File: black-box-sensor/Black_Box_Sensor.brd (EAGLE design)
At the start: 100 x 80 mm, 4 parts, among them U1 ADXL375, U2 ADXL375, U3 ATMEGA32U4-AU, U4 FXAS21002CQR1

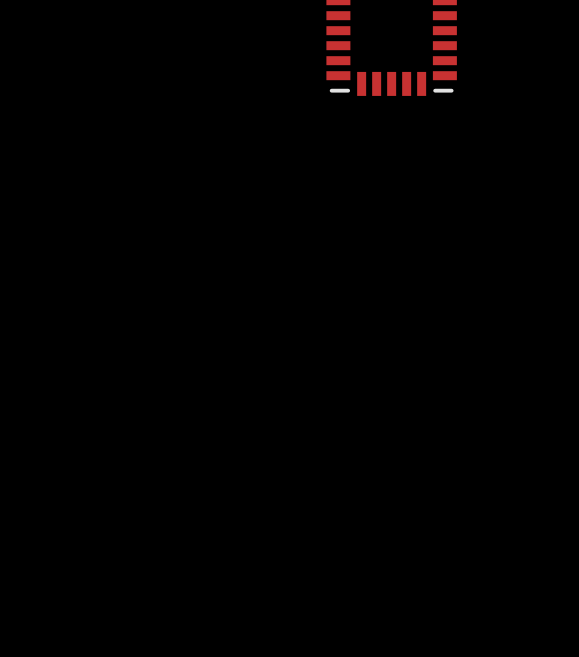
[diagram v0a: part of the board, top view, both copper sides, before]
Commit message: voltage regulator addition
added voltage reg to the library, and added appropriate parts to the schematic for the voltage regulator to work
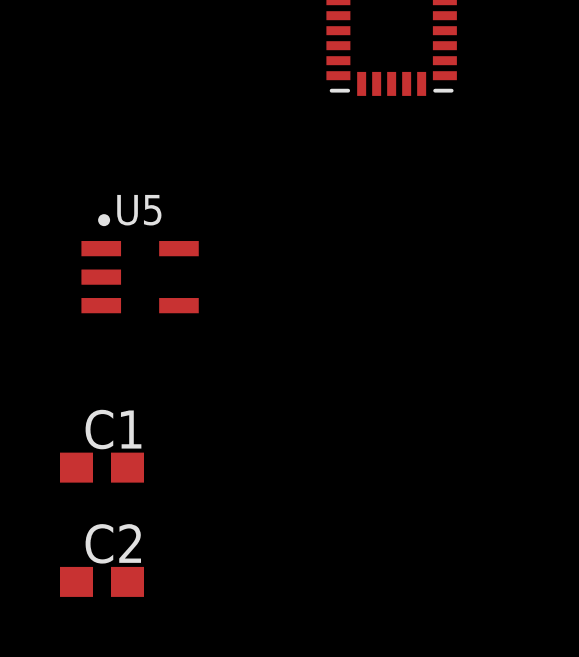
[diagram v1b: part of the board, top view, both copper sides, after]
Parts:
- added C1, C2: 1µF, rcl:C0603
- added U5: MIC5504-3.3YM5-TR, BBS_Library:SOT-23-5_MC_MCH
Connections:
- new net +3.3V: C2.1, U5.5
- new net GND: C1.2, C2.2, U5.2
- new net VBATT: C1.1, U5.1, U5.3
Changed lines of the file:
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@@
 <?xml version="1.0" encoding="utf-8"?>
 <!DOCTYPE eagle SYSTEM "eagle.dtd">
-<eagle version="9.6.2">
+<eagle version="9.5.1">
 <drawing>
 <settings>
@@
 <layers>
 <layer number="1" name="Top" color="4" fill="1" visible="yes" active="yes"/>
+<layer number="2" name="Route2" color="16" fill="1" visible="no" active="no"/>
+<layer number="3" name="Route3" color="17" fill="1" visible="no" active="no"/>
+<layer number="4" name="Route4" color="18" fill="1" visible="no" active="no"/>
+<layer number="5" name="Route5" color="19" fill="1" visible="no" active="no"/>
+<layer number="6" name="Route6" color="25" fill="1" visible="no" active="no"/>
+<layer number="7" name="Route7" color="26" fill="1" visible="no" active="no"/>
+<layer number="8" name="Route8" color="27" fill="1" visible="no" active="no"/>
+<layer number="9" name="Route9" color="28" fill="1" visible="no" active="no"/>
+<layer number="10" name="Route10" color="29" fill="1" visible="no" active="no"/>
+<layer number="11" name="Route11" color="30" fill="1" visible="no" active="no"/>
+<layer number="12" name="Route12" color="20" fill="1" visible="no" active="no"/>
+<layer number="13" name="Route13" color="21" fill="1" visible="no" active="no"/>
+<layer number="14" name="Route14" color="22" fill="1" visible="no" active="no"/>
+<layer number="15" name="Route15" color="23" fill="1" visible="no" active="no"/>
 <layer number="16" name="Bottom" color="1" fill="1" visible="yes" active="yes"/>
 <layer number="17" name="Pads" color="2" fill="1" visible="yes" active="yes"/>
@@
 <attribute name="VALUE" x="-4.275" y="-41.775" size="1" layer="27" font="vector" ratio="10" align="top-left"/>
 </element>
+<element name="U5" library="BBS_Library" package="SOT-23-5_MC_MCH" value="MIC5504-3.3YM5-TR" x="-10.16" y="-46.99" smashed="yes">
+<attribute name="DKPN" value="576-4764-1-ND" x="-10.16" y="-46.99" size="1.778" layer="27" display="off"/>
+<attribute name="NAME" x="-11.03" y="-45.25" size="1" layer="25" font="vector" ratio="10"/>
+<attribute name="VALUE" x="-11.13" y="-48.8" size="1" layer="27" font="vector" ratio="10" align="top-left"/>
+</element>
+<element name="C1" library="rcl" library_urn="urn:adsk.eagle:library:334" package="C0603" package3d_urn="urn:adsk.eagle:package:23616/2" value="1µF" x="-11.43" y="-53.34" smashed="yes">
+<attribute name="DKPN" value="CC0603KRX7R6BB105" x="-11.43" y="-53.34" size="1.778" layer="27" display="off"/>
+<attribute name="NAME" x="-12.065" y="-52.705" size="1.27" layer="25"/>
+<attribute name="POPULARITY" value="37" x="-11.43" y="-53.34" size="1.778" layer="27" display="off"/>
+<attribute name="SPICEPREFIX" value="C" x="-11.43" y="-53.34" size="1.778" layer="27" display="off"/>
+<attribute name="VALUE" x="-12.065" y="-55.245" size="1.27" layer="27"/>
+<attribute name="VOLTAGE" value="10V" x="-11.43" y="-53.34" size="1.778" layer="27" display="off"/>
+</element>
+<element name="C2" library="rcl" library_urn="urn:adsk.eagle:library:334" package="C0603" package3d_urn="urn:adsk.eagle:package:23616/2" value="1µF" x="-11.43" y="-57.15" smashed="yes">
+<attribute name="DKPN" value="CC0603KRX7R6BB105" x="-11.43" y="-57.15" size="1.778" layer="27" display="off"/>
+<attribute name="NAME" x="-12.065" y="-56.515" size="1.27" layer="25"/>
+<attribute name="POPULARITY" value="37" x="-11.43" y="-57.15" size="1.778" layer="27" display="off"/>
+<attribute name="SPICEPREFIX" value="C" x="-11.43" y="-57.15" size="1.778" layer="27" display="off"/>
+<attribute name="VALUE" x="-12.065" y="-59.055" size="1.27" layer="27"/>
+<attribute name="VOLTAGE" value="10V" x="-11.43" y="-57.15" size="1.778" layer="27" display="off"/>
+</element>
 </elements>
 <signals>
+<signal name="GND">
+<contactref element="U5" pad="2"/>
+<contactref element="C1" pad="2"/>
+<contactref element="C2" pad="2"/>
+<wire x1="-10.58" y1="-53.34" x2="-10.58" y2="-57.15" width="0" layer="19" extent="1-1"/>
+<wire x1="-11.4554" y1="-46.99" x2="-10.58" y2="-53.34" width="0" layer="19" extent="1-1"/>
+</signal>
+<signal name="VBATT">
+<contactref element="U5" pad="1"/>
+<contactref element="C1" pad="1"/>
+<contactref element="U5" pad="3"/>
+<wire x1="-11.4554" y1="-47.94" x2="-12.28" y2="-53.34" width="0" layer="19" extent="1-1"/>
+<wire x1="-11.4554" y1="-46.04" x2="-11.4554" y2="-47.94" width="0" layer="19" extent="1-1"/>
+</signal>
+<signal name="+3.3V">
+<contactref element="U5" pad="5"/>
+<contactref element="C2" pad="1"/>
+<wire x1="-8.8646" y1="-46.04" x2="-12.28" y2="-57.15" width="0" layer="19" extent="1-1"/>
+</signal>
 </signals>
 <mfgpreviewcolors>
@@
 </board>
 </drawing>
+<compatibility>
+<note version="8.2" severity="warning">
+Since Version 8.2, EAGLE supports online libraries. The ids
+of those online libraries will not be understood (or retained)
+with this version.
+</note>
+<note version="8.3" severity="warning">
+Since Version 8.3, EAGLE supports URNs for individual library
+assets (packages, symbols, and devices). The URNs of those assets
+will not be understood (or retained) with this version.
+</note>
+<note version="8.3" severity="warning">
+Since Version 8.3, EAGLE supports the association of 3D packages
+with devices in libraries, schematics, and board files. Those 3D
+packages will not be understood (or retained) with this version.
+</note>
+</compatibility>
 </eagle>

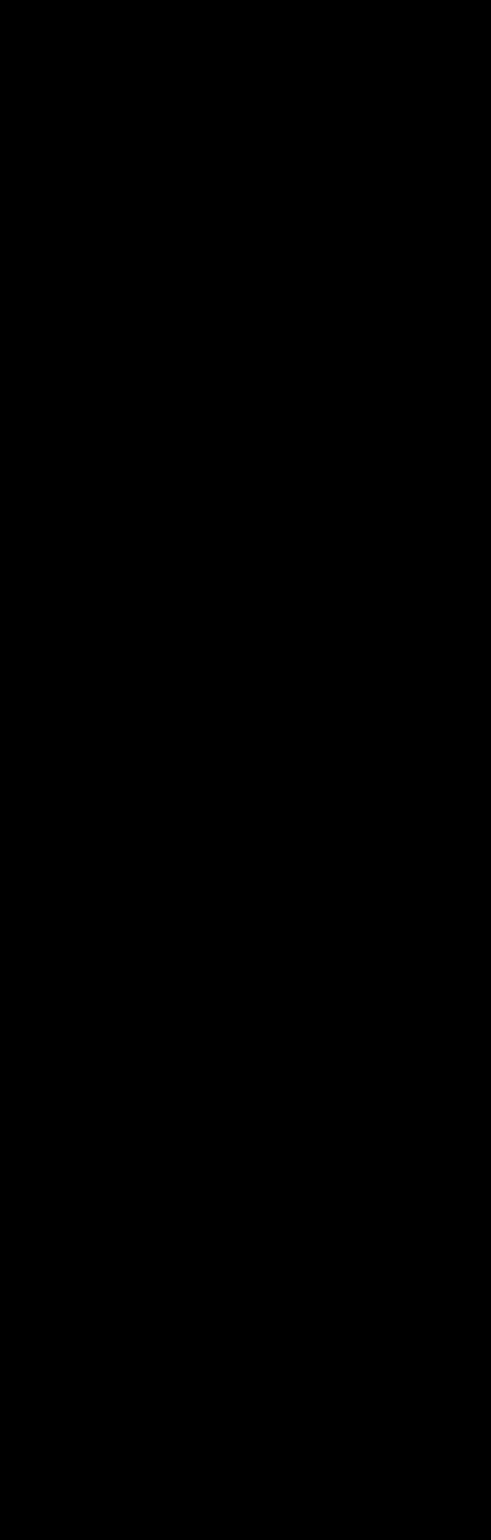
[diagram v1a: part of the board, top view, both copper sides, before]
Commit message: start schematic for accelerometer and gyro
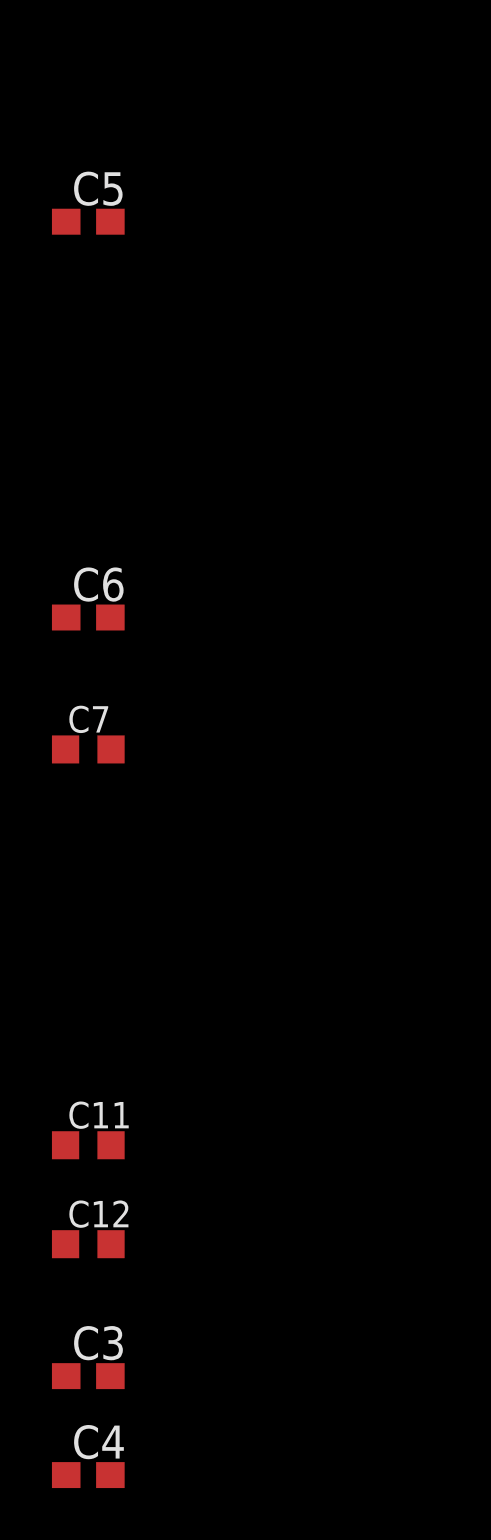
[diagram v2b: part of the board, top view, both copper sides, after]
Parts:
- added C11, C12: 0.1uF, rcl:C0603K
- added C3, C4: 0.1uF, rcl:C0603
- added C5: 10uF, rcl:C0603
- added C6: 100nF, rcl:C0603
- added C7: 1uF, rcl:C0603K
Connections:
- new net 3.3V: C11.1, C4.1, C7.1, U1.1, U4.15
- new net N$1: C6.1, U4.16
- new net N$2: C3.1, C5.1
- new net N$3: C12.1, U4.18, U4.8
- net GND: now also C11.2, C12.2, C3.2, C4.2, C5.2, C6.2, C7.2, U1.2, U1.4, U1.5, U1.6, U4.1, U4.10, U4.14, U4.19, U4.20, U4.21, U4.22, U4.23, U4.24, U4.5, U4.6, U4.7, U4.9
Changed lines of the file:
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@@
 <?xml version="1.0" encoding="utf-8"?>
 <!DOCTYPE eagle SYSTEM "eagle.dtd">
-<eagle version="9.5.1">
+<eagle version="9.6.2">
 <drawing>
 <settings>
@@
 <attribute name="VOLTAGE" value="10V" x="-11.43" y="-57.15" size="1.778" layer="27" display="off"/>
 </element>
+<element name="C5" library="rcl" library_urn="urn:adsk.eagle:library:334" package="C0603" package3d_urn="urn:adsk.eagle:package:23616/2" value="10uF" x="-11.43" y="-71.12" smashed="yes">
+<attribute name="NAME" x="-12.065" y="-70.485" size="1.27" layer="25"/>
+<attribute name="POPULARITY" value="37" x="-11.43" y="-71.12" size="1.778" layer="27" display="off"/>
+<attribute name="SPICEPREFIX" value="C" x="-11.43" y="-71.12" size="1.778" layer="27" display="off"/>
+<attribute name="VALUE" x="-12.065" y="-73.025" size="1.27" layer="27"/>
+</element>
+<element name="C6" library="rcl" library_urn="urn:adsk.eagle:library:334" package="C0603" package3d_urn="urn:adsk.eagle:package:23616/2" value="100nF" x="-11.43" y="-86.36" smashed="yes">
+<attribute name="NAME" x="-12.065" y="-85.725" size="1.27" layer="25"/>
+<attribute name="POPULARITY" value="37" x="-11.43" y="-86.36" size="1.778" layer="27" display="off"/>
+<attribute name="SPICEPREFIX" value="C" x="-11.43" y="-86.36" size="1.778" layer="27" display="off"/>
+<attribute name="VALUE" x="-12.065" y="-88.265" size="1.27" layer="27"/>
+</element>
+<element name="C7" library="rcl" library_urn="urn:adsk.eagle:library:334" package="C0603K" package3d_urn="urn:adsk.eagle:package:23680/2" value="1uF" x="-11.43" y="-91.44" smashed="yes">
+<attribute name="NAME" x="-12.23" y="-90.79" size="1.016" layer="25"/>
+<attribute name="POPULARITY" value="5" x="-11.43" y="-91.44" size="1.778" layer="27" display="off"/>
+<attribute name="SPICEPREFIX" value="C" x="-11.43" y="-91.44" size="1.778" layer="27" display="off"/>
+<attribute name="VALUE" x="-12.23" y="-93.09" size="1.016" layer="27"/>
+</element>
+<element name="C11" library="rcl" library_urn="urn:adsk.eagle:library:334" package="C0603K" package3d_urn="urn:adsk.eagle:package:23680/2" value="0.1uF" x="-11.43" y="-106.68" smashed="yes">
+<attribute name="NAME" x="-12.23" y="-106.03" size="1.016" layer="25"/>
+<attribute name="POPULARITY" value="5" x="-11.43" y="-106.68" size="1.778" layer="27" display="off"/>
+<attribute name="SPICEPREFIX" value="C" x="-11.43" y="-106.68" size="1.778" layer="27" display="off"/>
+<attribute name="VALUE" x="-12.23" y="-108.33" size="1.016" layer="27"/>
+</element>
+<element name="C12" library="rcl" library_urn="urn:adsk.eagle:library:334" package="C0603K" package3d_urn="urn:adsk.eagle:package:23680/2" value="0.1uF" x="-11.43" y="-110.49" smashed="yes">
+<attribute name="NAME" x="-12.23" y="-109.84" size="1.016" layer="25"/>
+<attribute name="POPULARITY" value="5" x="-11.43" y="-110.49" size="1.778" layer="27" display="off"/>
+<attribute name="SPICEPREFIX" value="C" x="-11.43" y="-110.49" size="1.778" layer="27" display="off"/>
+<attribute name="VALUE" x="-12.23" y="-112.14" size="1.016" layer="27"/>
+</element>
+<element name="C3" library="rcl" library_urn="urn:adsk.eagle:library:334" package="C0603" package3d_urn="urn:adsk.eagle:package:23616/2" value="0.1uF" x="-11.43" y="-115.57" smashed="yes">
+<attribute name="NAME" x="-12.065" y="-114.935" size="1.27" layer="25"/>
+<attribute name="POPULARITY" value="37" x="-11.43" y="-115.57" size="1.778" layer="27" display="off"/>
+<attribute name="SPICEPREFIX" value="C" x="-11.43" y="-115.57" size="1.778" layer="27" display="off"/>
+<attribute name="VALUE" x="-12.065" y="-117.475" size="1.27" layer="27"/>
+</element>
+<element name="C4" library="rcl" library_urn="urn:adsk.eagle:library:334" package="C0603" package3d_urn="urn:adsk.eagle:package:23616/2" value="0.1uF" x="-11.43" y="-119.38" smashed="yes">
+<attribute name="NAME" x="-12.065" y="-118.745" size="1.27" layer="25"/>
+<attribute name="POPULARITY" value="37" x="-11.43" y="-119.38" size="1.778" layer="27" display="off"/>
+<attribute name="SPICEPREFIX" value="C" x="-11.43" y="-119.38" size="1.778" layer="27" display="off"/>
+<attribute name="VALUE" x="-12.065" y="-121.285" size="1.27" layer="27"/>
+</element>
 </elements>
 <signals>
@@
 <contactref element="C1" pad="2"/>
 <contactref element="C2" pad="2"/>
+<contactref element="U1" pad="2"/>
+<contactref element="U1" pad="5"/>
+<contactref element="U1" pad="4"/>
+<contactref element="C5" pad="2"/>
+<contactref element="U4" pad="1" route="any" routetag="G$1.GND"/>
+<contactref element="U4" pad="5" route="any" routetag="G$1.GND"/>
+<contactref element="U4" pad="14" route="any" routetag="G$1.GND"/>
+<contactref element="U4" pad="19" route="any" routetag="G$1.GND"/>
+<contactref element="U4" pad="23"/>
+<contactref element="U4" pad="10"/>
+<contactref element="U4" pad="24"/>
+<contactref element="U4" pad="9"/>
+<contactref element="U4" pad="7"/>
+<contactref element="U4" pad="20"/>
+<contactref element="U4" pad="21"/>
+<contactref element="U4" pad="6"/>
+<contactref element="U4" pad="22"/>
+<contactref element="C6" pad="2"/>
+<contactref element="C7" pad="2"/>
+<contactref element="C3" pad="2"/>
+<contactref element="C4" pad="2"/>
+<contactref element="U1" pad="6"/>
+<contactref element="C11" pad="2"/>
+<contactref element="C12" pad="2"/>
+<wire x1="-10.58" y1="-115.57" x2="-10.58" y2="-119.38" width="0" layer="19" extent="1-1"/>
+<wire x1="-10.555" y1="-110.49" x2="-10.58" y2="-115.57" width="0" layer="19" extent="1-1"/>
+<wire x1="-10.555" y1="-106.68" x2="-10.555" y2="-110.49" width="0" layer="19" extent="1-1"/>
+<wire x1="-10.555" y1="-91.44" x2="-10.555" y2="-106.68" width="0" layer="19" extent="1-1"/>
+<wire x1="-10.58" y1="-86.36" x2="-10.555" y2="-91.44" width="0" layer="19" extent="1-1"/>
+<wire x1="-10.58" y1="-71.12" x2="-10.58" y2="-86.36" width="0" layer="19" extent="1-1"/>
+<wire x1="-10.58" y1="-57.15" x2="-10.58" y2="-71.12" width="0" layer="19" extent="1-1"/>
 <wire x1="-10.58" y1="-53.34" x2="-10.58" y2="-57.15" width="0" layer="19" extent="1-1"/>
 <wire x1="-11.4554" y1="-46.99" x2="-10.58" y2="-53.34" width="0" layer="19" extent="1-1"/>
+<wire x1="-3.55" y1="-40.275" x2="-11.4554" y2="-46.99" width="0" layer="19" extent="1-1"/>
+<wire x1="-3.55" y1="-39.775" x2="-3.55" y2="-40.275" width="0" layer="19" extent="1-1"/>
+<wire x1="-3.55" y1="-39.275" x2="-3.55" y2="-39.775" width="0" layer="19" extent="1-1"/>
+<wire x1="-2.775" y1="-37" x2="-3.55" y2="-37.275" width="0" layer="19" extent="1-1"/>
+<wire x1="-2.275" y1="-37" x2="-2.775" y2="-37" width="0" layer="19" extent="1-1"/>
+<wire x1="-1.775" y1="-37" x2="-2.275" y2="-37" width="0" layer="19" extent="1-1"/>
+<wire x1="-1.275" y1="-37" x2="-1.775" y2="-37" width="0" layer="19" extent="1-1"/>
+<wire x1="-0.775" y1="-37" x2="-1.275" y2="-37" width="0" layer="19" extent="1-1"/>
+<wire x1="-2.275" y1="-40.55" x2="-3.55" y2="-40.275" width="0" layer="19" extent="1-1"/>
+<wire x1="-1.775" y1="-40.55" x2="-2.275" y2="-40.55" width="0" layer="19" extent="1-1"/>
+<wire x1="-4.9075" y1="4.35" x2="-2.775" y2="-37" width="0" layer="19" extent="1-1"/>
+<wire x1="-4.9075" y1="5.15" x2="-4.9075" y2="4.35" width="0" layer="19" extent="1-1"/>
+<wire x1="-4.9075" y1="5.95" x2="-4.9075" y2="5.15" width="0" layer="19" extent="1-1"/>
+<wire x1="-4.9075" y1="7.55" x2="-4.9075" y2="5.95" width="0" layer="19" extent="1-1"/>
 </signal>
 <signal name="VBATT">
@@
 <wire x1="-8.8646" y1="-46.04" x2="-12.28" y2="-57.15" width="0" layer="19" extent="1-1"/>
 </signal>
+<signal name="3.3V">
+<contactref element="U1" pad="1"/>
+<contactref element="C4" pad="1"/>
+<contactref element="C11" pad="1"/>
+<contactref element="C7" pad="1"/>
+<contactref element="U4" pad="15"/>
+<wire x1="-12.305" y1="-106.68" x2="-12.28" y2="-119.38" width="0" layer="19" extent="1-1"/>
+<wire x1="-12.305" y1="-91.44" x2="-12.305" y2="-106.68" width="0" layer="19" extent="1-1"/>
+<wire x1="0" y1="-39.275" x2="-12.305" y2="-91.44" width="0" layer="19" extent="1-1"/>
+<wire x1="-4.9075" y1="8.35" x2="0" y2="-39.275" width="0" layer="19" extent="1-1"/>
+</signal>
+<signal name="N$1">
+<contactref element="U4" pad="16"/>
+<contactref element="C6" pad="1"/>
+<wire x1="0" y1="-38.775" x2="-12.28" y2="-86.36" width="0" layer="19" extent="1-1"/>
+</signal>
+<signal name="N$2">
+<contactref element="C3" pad="1"/>
+<contactref element="C5" pad="1"/>
+<wire x1="-12.28" y1="-71.12" x2="-12.28" y2="-115.57" width="0" layer="19" extent="1-1"/>
+</signal>
+<signal name="N$3">
+<contactref element="U4" pad="18"/>
+<contactref element="C12" pad="1"/>
+<contactref element="U4" pad="8"/>
+<wire x1="-2.775" y1="-40.55" x2="-12.305" y2="-110.49" width="0" layer="19" extent="1-1"/>
+<wire x1="0" y1="-37.775" x2="-2.775" y2="-40.55" width="0" layer="19" extent="1-1"/>
+</signal>
 </signals>

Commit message: quick meeting edits
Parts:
- removed C5: 10uF, rcl:C0603
- removed C7: 1uF, rcl:C0603K
- added U6: NL27WZ32USG, Hocki_Library:US8
- moved C1 79.7 mm to (19.1, 20.3), turned to 90 degrees
- moved C2 76.7 mm to (14.0, 15.2), turned to 180 degrees
- moved U4 59.9 mm to (16.0, 18.4)
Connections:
- removed net N$2: C3.1, C5.1
- removed net N$3: C12.1, U4.18, U4.8
- net 3.3V: now also C12.1, C3.1, U4.18, U4.4, U4.8; no longer C7.1
- net GND: no longer C5.2, C7.2
